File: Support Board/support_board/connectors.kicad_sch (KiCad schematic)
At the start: 7 parts, among them J41 GPS_CONN, J42 POWER_CONN, J43 TELEM2_CONN1, J44 Conn_01x04_Socket, J45 SWITCH_DEBUG, J46 TELEM2_DEBUG, J47 SWITCH_CONN

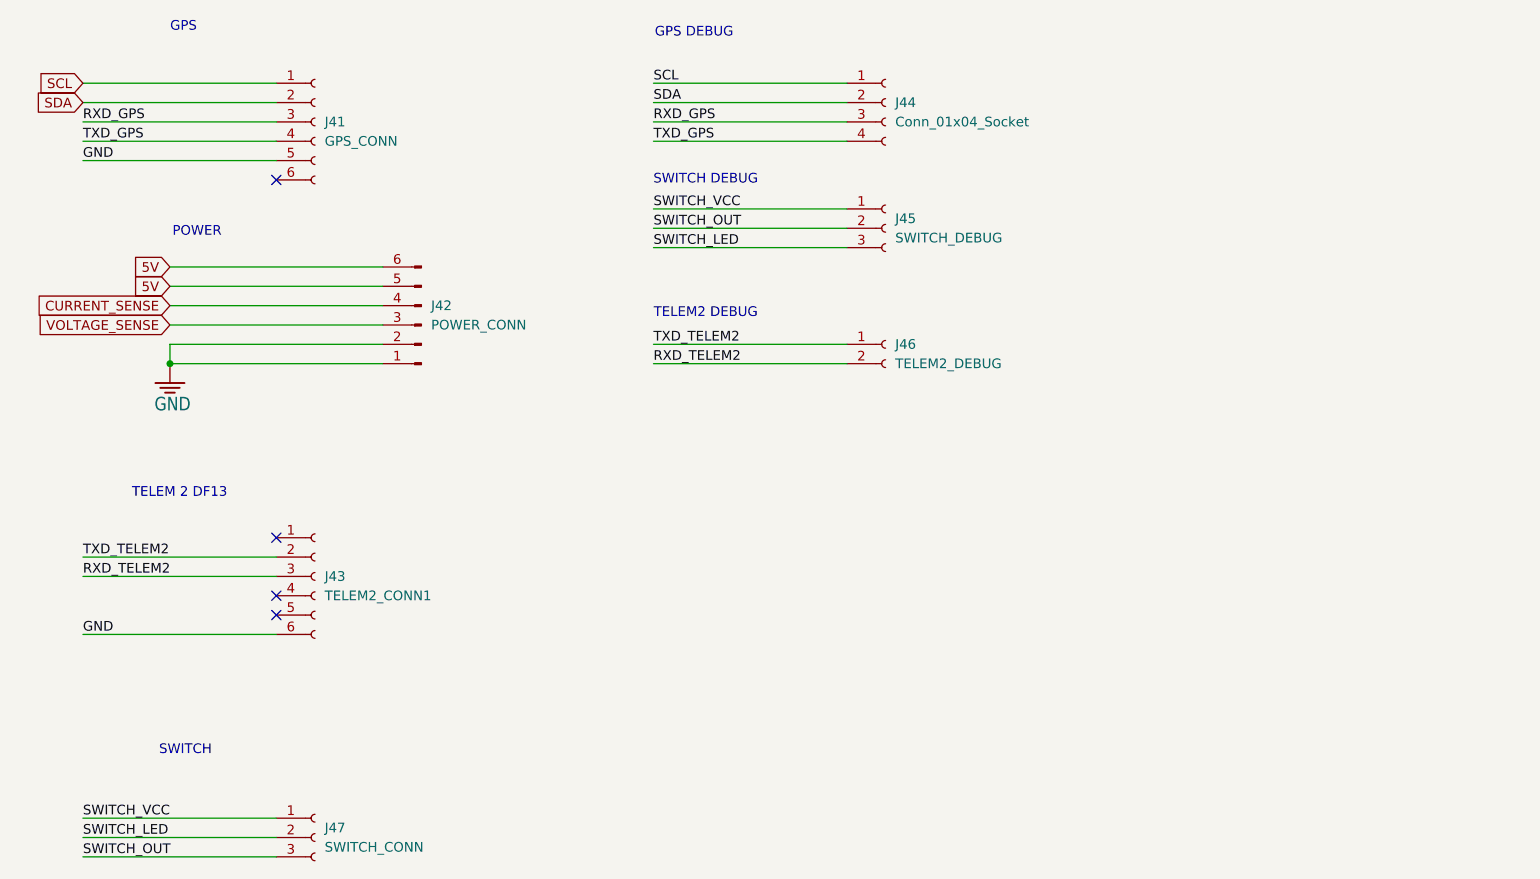
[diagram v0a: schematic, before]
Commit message: Updated PM files and Schematics in the Support Board
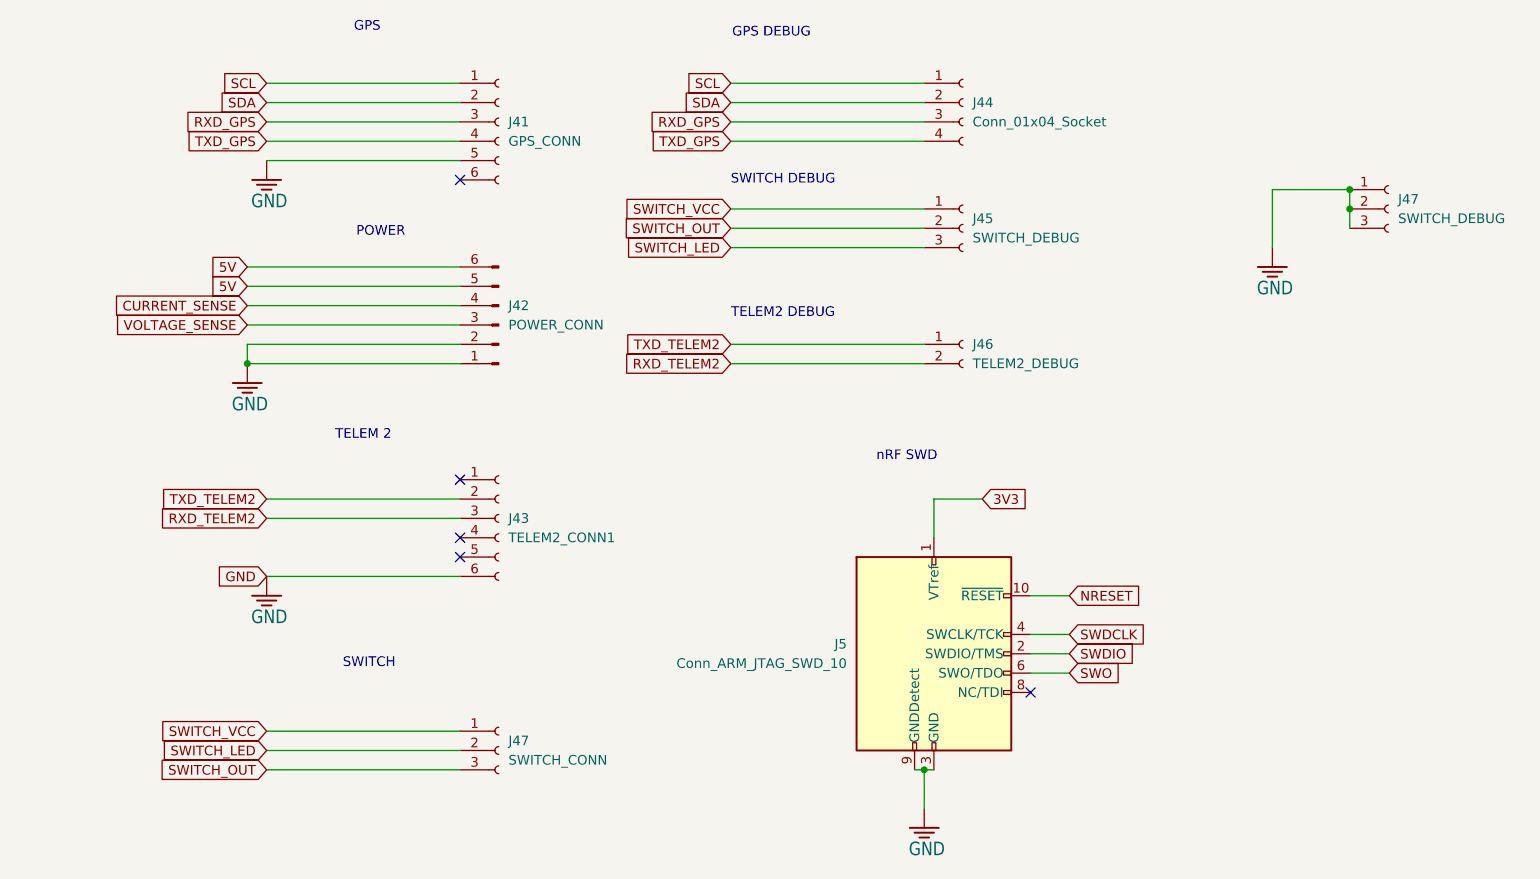
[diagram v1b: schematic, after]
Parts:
- added J47: SWITCH_DEBUG, Connector_Wire:SolderWire-0.75sqmm_1x03_P7mm_D1.25mm_OD3.5mm, symbol Connector:Conn_01x03_Socket
- added J5: Conn_ARM_JTAG_SWD_10, symbol Connector:Conn_ARM_JTAG_SWD_10
- J44: footprint Connector_JST:JST_EH_B4B-EH-A_1x04_P2.50mm_Vertical -> Connector_Wire:SolderWire-0.75sqmm_1x04_P4.8mm_D1.25mm_OD2.3mm
- J45: footprint Connector_JST:JST_EH_B3B-EH-A_1x03_P2.50mm_Vertical -> Connector_Wire:SolderWire-0.75sqmm_1x03_P7mm_D1.25mm_OD3.5mm
- J46: footprint Connector_JST:JST_EH_B2B-EH-A_1x02_P2.50mm_Vertical -> Connector_Wire:SolderWire-0.75sqmm_1x02_P7mm_D1.25mm_OD3.5mm
- J47: footprint Connector_Hirose:Hirose_DF13-03P-1.25DSA_1x03_P1.25mm_Vertical -> Connector_JST:JST_EH_B3B-EH-A_1x03_P2.50mm_Vertical
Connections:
- net GND: now also J47.1 (Pin_1), J47.2 (Pin_2), J47.3 (Pin_3), J5.3 (GND), J5.5 (GND), J5.9 (GNDDetect)
- new net 3V3: J5.1 (VTref)
- new net NRESET: J5.10 (~{RESET})
- new net SWDCLK: J5.4 (SWCLK/TCK)
- new net SWDIO: J5.2 (SWDIO/TMS)
- new net SWO: J5.6 (SWO/TDO)
- no-connect marks 4 -> 5
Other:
- note added: "TELEM 2"
- note added: "nRF SWD"
- note removed: "TELEM 2 DF13"
- moved on the sheet: J41, J42, J43, J44, J45, J46, J47
